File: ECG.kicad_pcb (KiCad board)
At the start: 2 copper layers, 65 parts, among them J1 SJ-3566AN, J2 Conn_01x02_Male, P1 MountingHole_Pad, P2 MountingHole_Pad, P3 MountingHole_Pad, Q1 MMBT3904-7-F, U1 ADR4525, U2 SP6641, U3 INA333, U4 OPA388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

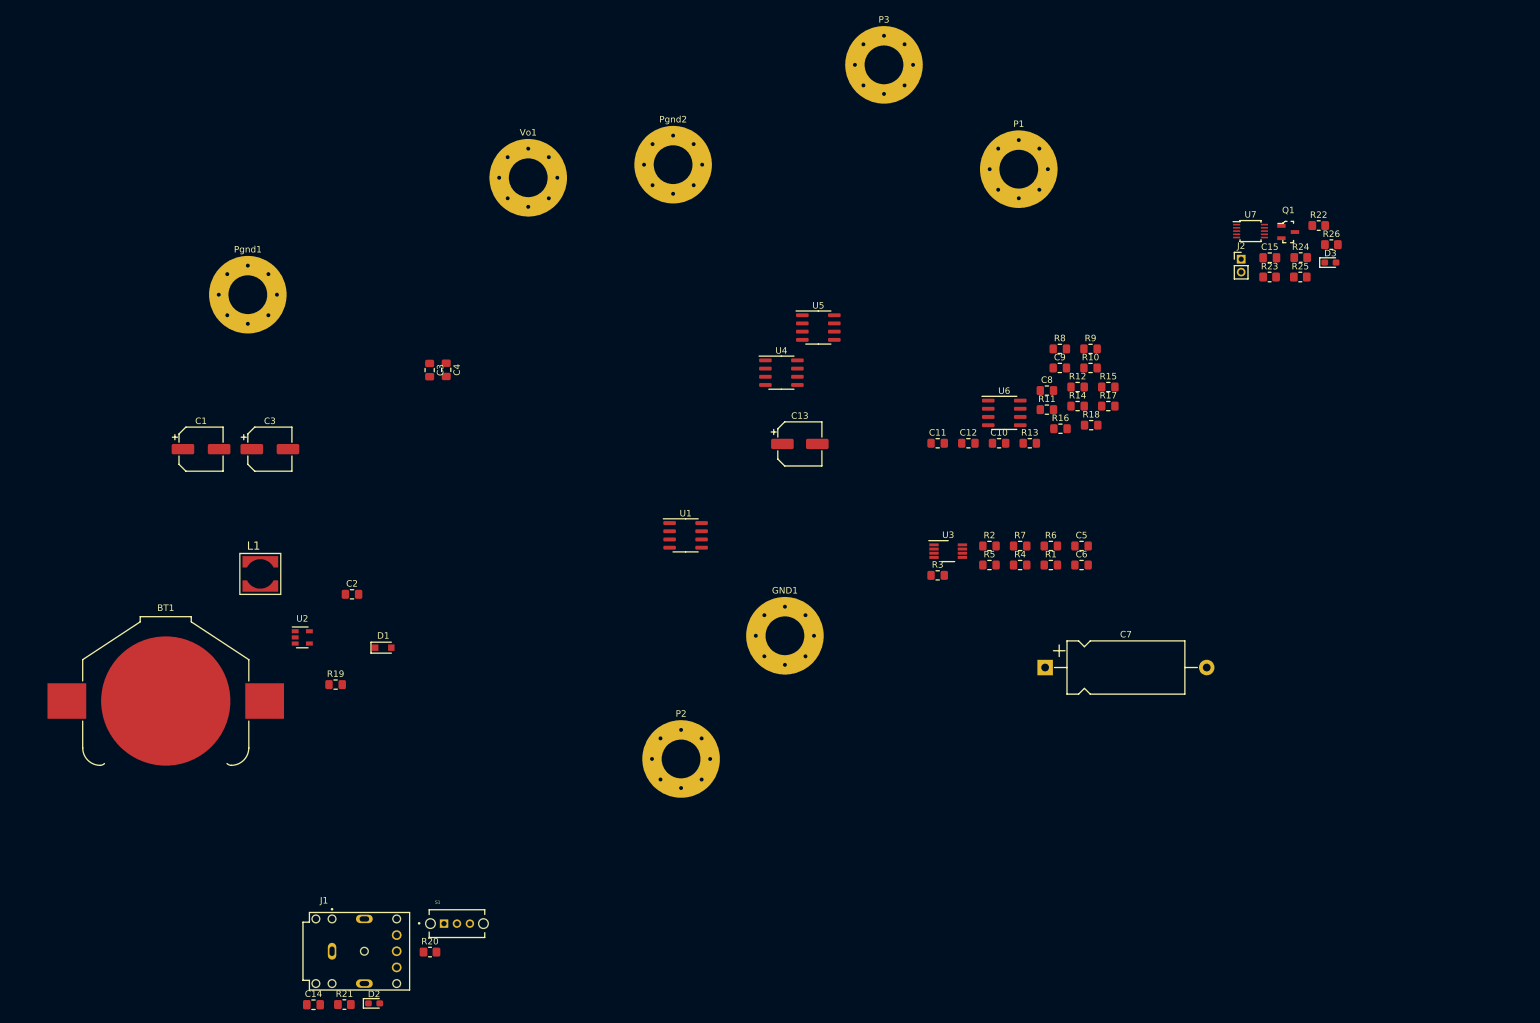
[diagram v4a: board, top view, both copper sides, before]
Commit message: #8 - Add test points. (Also updated filter circuit)
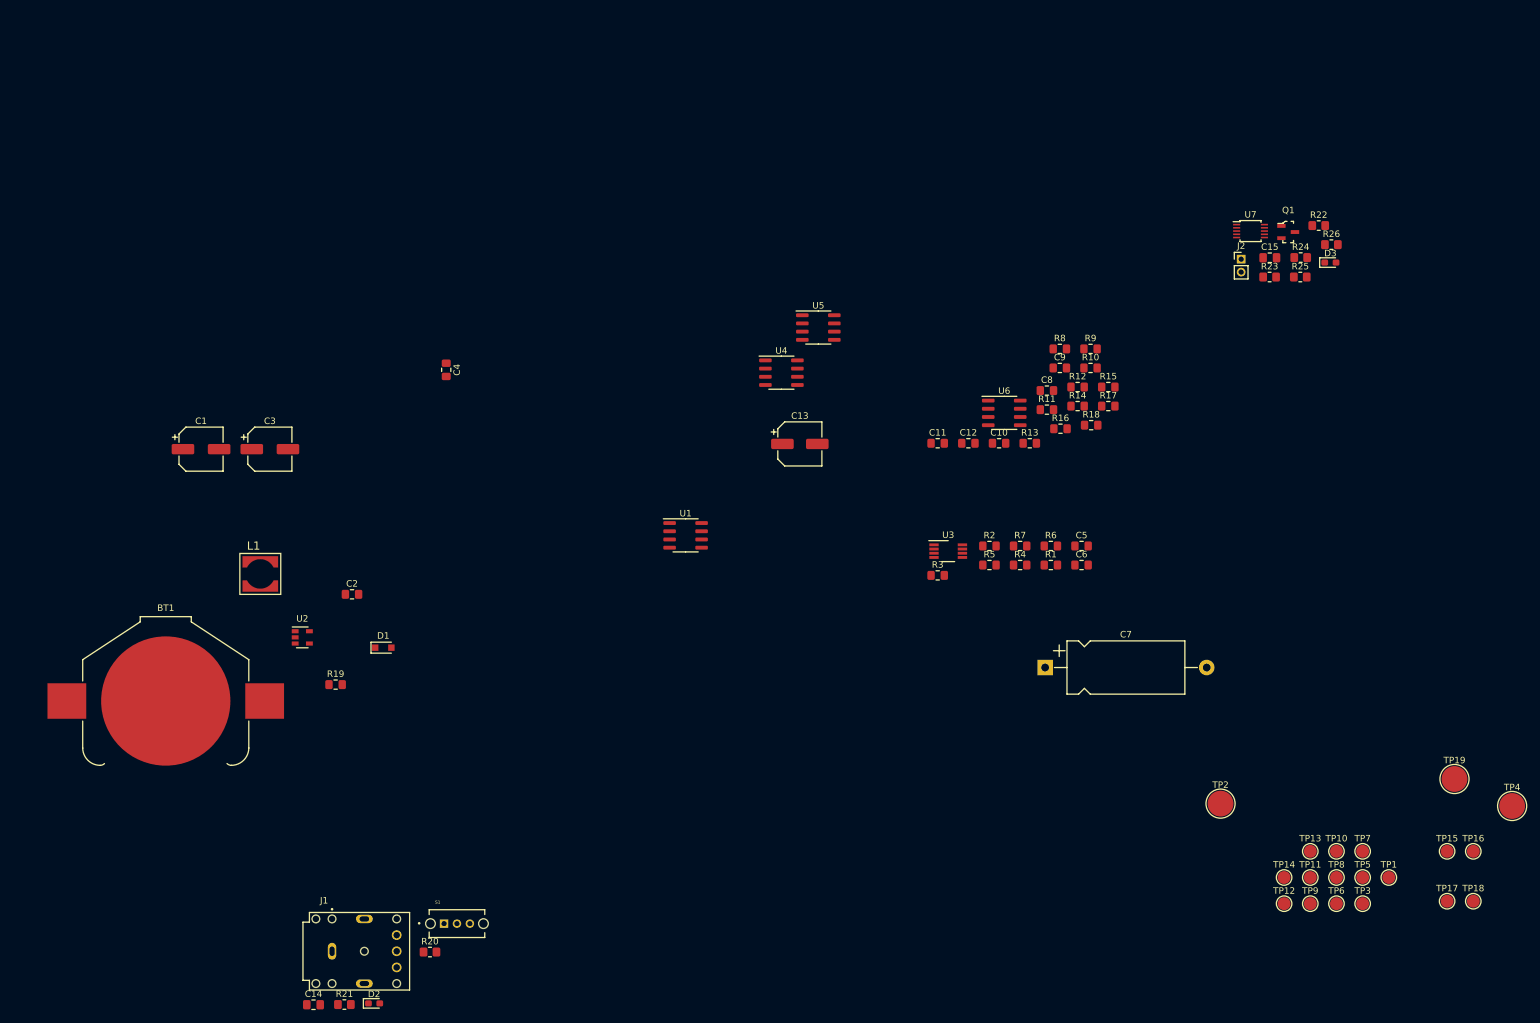
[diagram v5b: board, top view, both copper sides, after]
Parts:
- removed the C3 at (95.4, 73.3)
- removed GND1, P1, P2, P3, Pgnd1, Pgnd2, Vo1: MountingHole_Pad, MountingHole:MountingHole_6mm_Pad_Via
- added TP1: TestPoint, TestPoint:TestPoint_Pad_D2.0mm, F.Cu at (243.8, 151.8)
- added TP10: TestPoint, TestPoint:TestPoint_Pad_D2.0mm, F.Cu at (235.7, 147.7)
- added TP11: TestPoint, TestPoint:TestPoint_Pad_D2.0mm, F.Cu at (231.7, 151.8)
- added TP12: TestPoint, TestPoint:TestPoint_Pad_D2.0mm, F.Cu at (227.6, 155.8)
- added TP13: TestPoint, TestPoint:TestPoint_Pad_D2.0mm, F.Cu at (231.7, 147.7)
- added TP14: TestPoint, TestPoint:TestPoint_Pad_D2.0mm, F.Cu at (227.6, 151.8)
- added TP15: TestPoint, TestPoint:TestPoint_Pad_D2.0mm, F.Cu at (252.9, 147.7)
- added TP16: TestPoint, TestPoint:TestPoint_Pad_D2.0mm, F.Cu at (256.9, 147.7)
- added TP17: TestPoint, TestPoint:TestPoint_Pad_D2.0mm, F.Cu at (252.9, 155.4)
- added TP18: TestPoint, TestPoint:TestPoint_Pad_D2.0mm, F.Cu at (256.9, 155.4)
- added TP19: TestPoint, TestPoint:TestPoint_Pad_D4.0mm, F.Cu at (254.0, 136.5)
- added TP2: TestPoint, TestPoint:TestPoint_Pad_D4.0mm, F.Cu at (217.8, 140.3)
- added TP3: TestPoint, TestPoint:TestPoint_Pad_D2.0mm, F.Cu at (239.8, 155.8)
- added TP4: TestPoint, TestPoint:TestPoint_Pad_D4.0mm, F.Cu at (262.9, 140.7)
- added TP5: TestPoint, TestPoint:TestPoint_Pad_D2.0mm, F.Cu at (239.8, 151.8)
- added TP6: TestPoint, TestPoint:TestPoint_Pad_D2.0mm, F.Cu at (235.7, 155.8)
- added TP7: TestPoint, TestPoint:TestPoint_Pad_D2.0mm, F.Cu at (239.8, 147.7)
- added TP8: TestPoint, TestPoint:TestPoint_Pad_D2.0mm, F.Cu at (235.7, 151.8)
- added TP9: TestPoint, TestPoint:TestPoint_Pad_D2.0mm, F.Cu at (231.7, 155.8)
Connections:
- C12 pad 1: Net-(C11-Pad1) -> Net-(C12-Pad1)
- R12 pad 2: Net-(R12-Pad2) -> Net-(C12-Pad1)
- R9 pad 1: Net-(R12-Pad2) -> Net-(C12-Pad1)

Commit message: #4 - Added the heart edge cut and updated the Kicad footprints that were removed
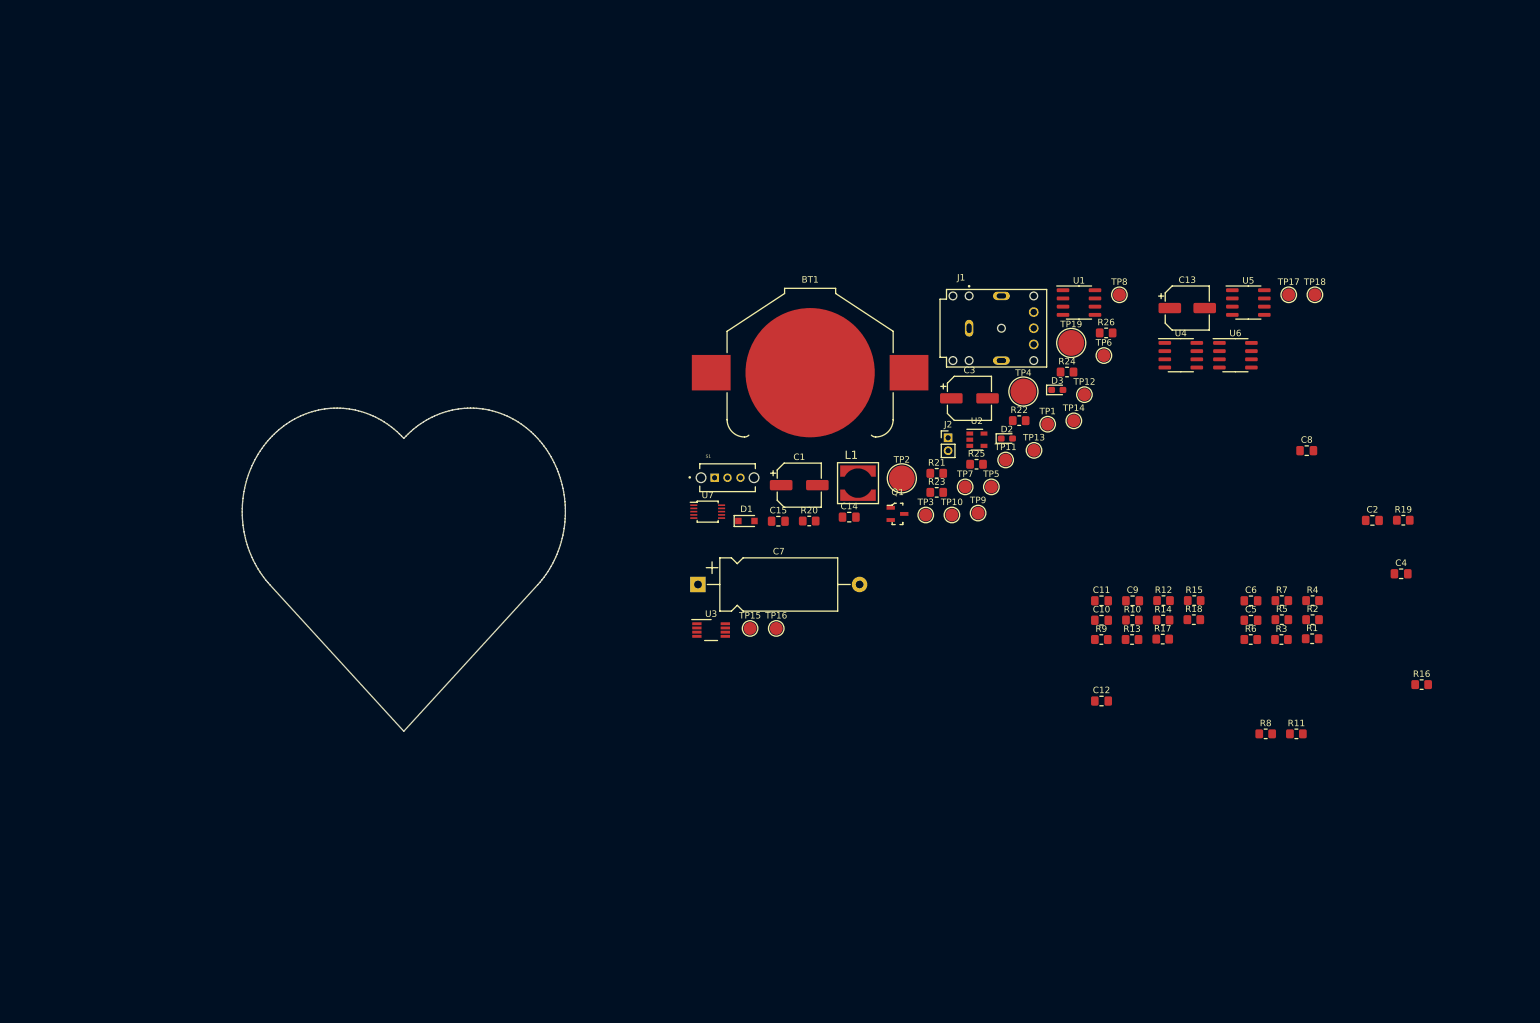
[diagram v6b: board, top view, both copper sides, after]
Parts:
- C10, C11, C12, C2, C4, C5, C6, C8, C9: footprint Capacitor_SMD:C_0805_2012Metric_Pad1.15x1.40mm_HandSolder -> Capacitor_SMD:C_0805_2012Metric_Pad1.18x1.45mm_HandSolder
- R1, R10, R11, R12, R13, R14, R15, R16, R17, R18, R19, R2, R3, R4, R5, R6, R7, R8, R9: footprint Resistor_SMD:R_0805_2012Metric_Pad1.15x1.40mm_HandSolder -> Resistor_SMD:R_0805_2012Metric_Pad1.20x1.40mm_HandSolder
- moved R19 167.1 mm to (246.1, 96.5)
- moved C2 158.3 mm to (241.3, 96.5)
- moved C4 151.1 mm to (245.7, 104.8), turned to 0 degrees
- moved J1 137.9 mm to (183.9, 66.8)
- moved D2 131.2 mm to (184.8, 83.8)
- moved R21 123.1 mm to (173.9, 89.2)
- moved TP15 113.2 mm to (145.0, 113.2)
- moved TP16 113.2 mm to (149.1, 113.2)
- moved C14 112.1 mm to (160.4, 96.0)
- moved BT1 111.9 mm to (154.3, 73.7)
- moved U2 108.8 mm to (180.1, 84.0)
- moved C3 108.5 mm to (179.0, 77.6)
- moved TP4 99.1 mm to (187.3, 76.6)
- moved TP17 97.0 mm to (228.4, 61.6)
- moved TP18 97.0 mm to (232.4, 61.6)
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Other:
- board outline added: 50 x 50 mm
- net class Default: clearance 0.1524 -> 0.2; trace_width 0.2032 -> 0.25; via_dia 0.6858 -> 0.6; via_drill 0.3302 -> 0.4
- rule pad_to_mask_clearance: 0.05 -> 0.2
- rule trace_clearance: 0.1524 -> 0.2

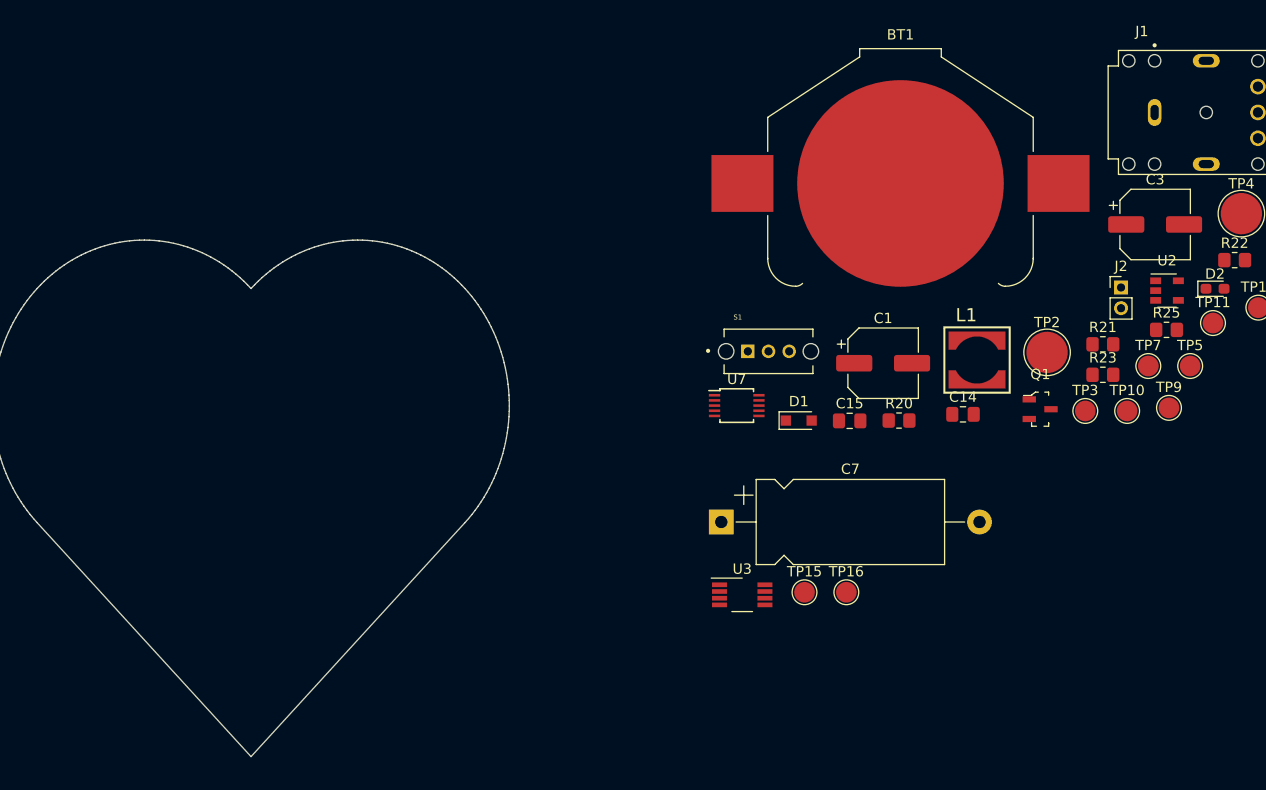
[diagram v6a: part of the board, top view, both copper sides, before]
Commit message: Added bypass cap to Vref input
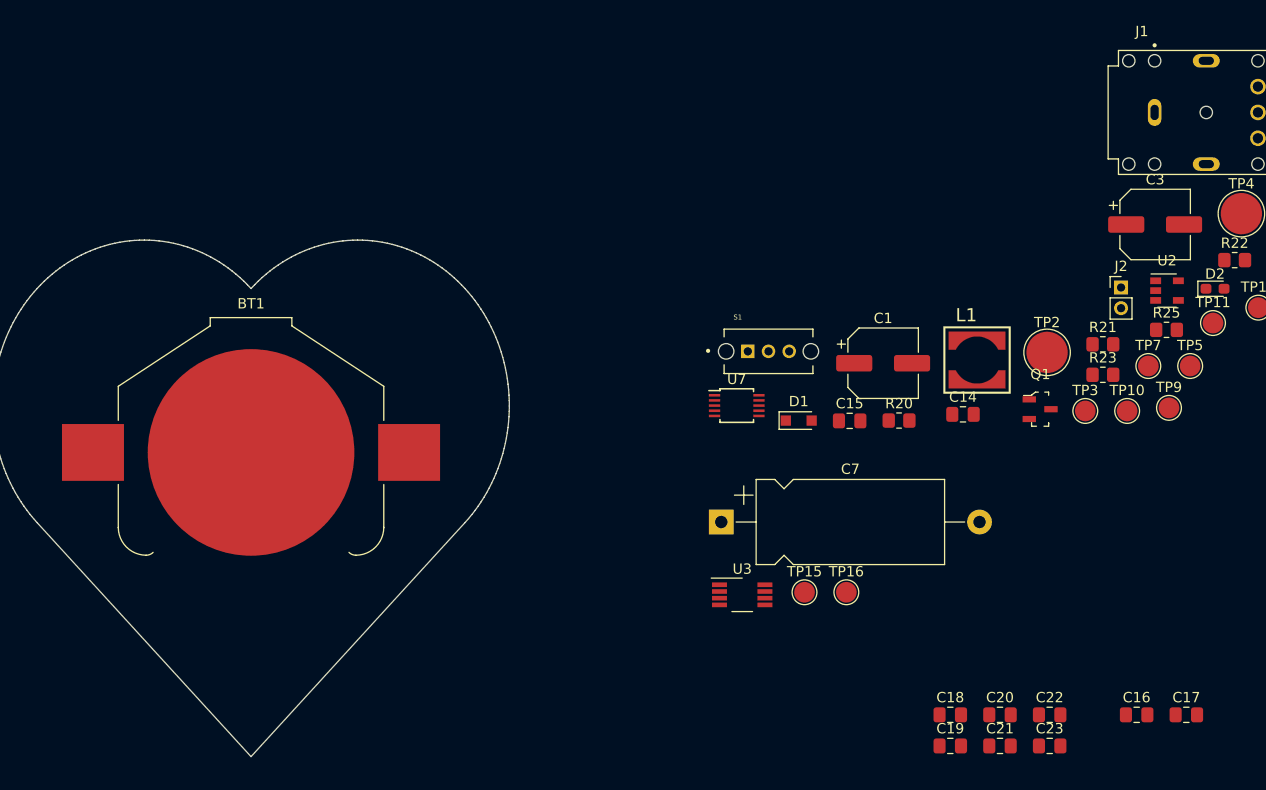
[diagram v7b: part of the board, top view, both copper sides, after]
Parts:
- added C16: 100n, Capacitor_SMD:C_0805_2012Metric_Pad1.18x1.45mm_HandSolder, F.Cu at (177.2, 125.1)
- added C17: 100n, Capacitor_SMD:C_0805_2012Metric_Pad1.18x1.45mm_HandSolder, F.Cu at (182.0, 125.1)
- added C18: 100n, Capacitor_SMD:C_0805_2012Metric_Pad1.18x1.45mm_HandSolder, F.Cu at (159.1, 125.1)
- added C19: 100n, Capacitor_SMD:C_0805_2012Metric_Pad1.18x1.45mm_HandSolder, F.Cu at (159.1, 128.1)
- added C20: 100n, Capacitor_SMD:C_0805_2012Metric_Pad1.18x1.45mm_HandSolder, F.Cu at (163.9, 125.1)
- added C21: 100n, Capacitor_SMD:C_0805_2012Metric_Pad1.18x1.45mm_HandSolder, F.Cu at (163.9, 128.1)
- added C22: 100n, Capacitor_SMD:C_0805_2012Metric_Pad1.18x1.45mm_HandSolder, F.Cu at (168.7, 125.1)
- added C23: 100n, Capacitor_SMD:C_0805_2012Metric_Pad1.18x1.45mm_HandSolder, F.Cu at (168.7, 128.1)
- C7: value CP1 -> 100u
- R16: value 3k -> 3.3k
- moved BT1 68.0 mm to (91.4, 99.7)
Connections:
- BT1 pad 1: Net-(BT1-Pad1) -> Vbatt
- C1 pad 1: Net-(BT1-Pad1) -> Vbatt
- J1 pad 6: 5V -> Vbatt
- L1 pad 1: Net-(BT1-Pad1) -> Vbatt
- TP1 pad 1: Net-(BT1-Pad1) -> Vbatt
- U2 pad 5: Net-(BT1-Pad1) -> Vbatt
